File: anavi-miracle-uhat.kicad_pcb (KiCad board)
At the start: 2 copper layers, 65 x 30 mm, 25 parts, among them U1 CAT24C32WI-GT3, U2 74LVC1G17W5-7

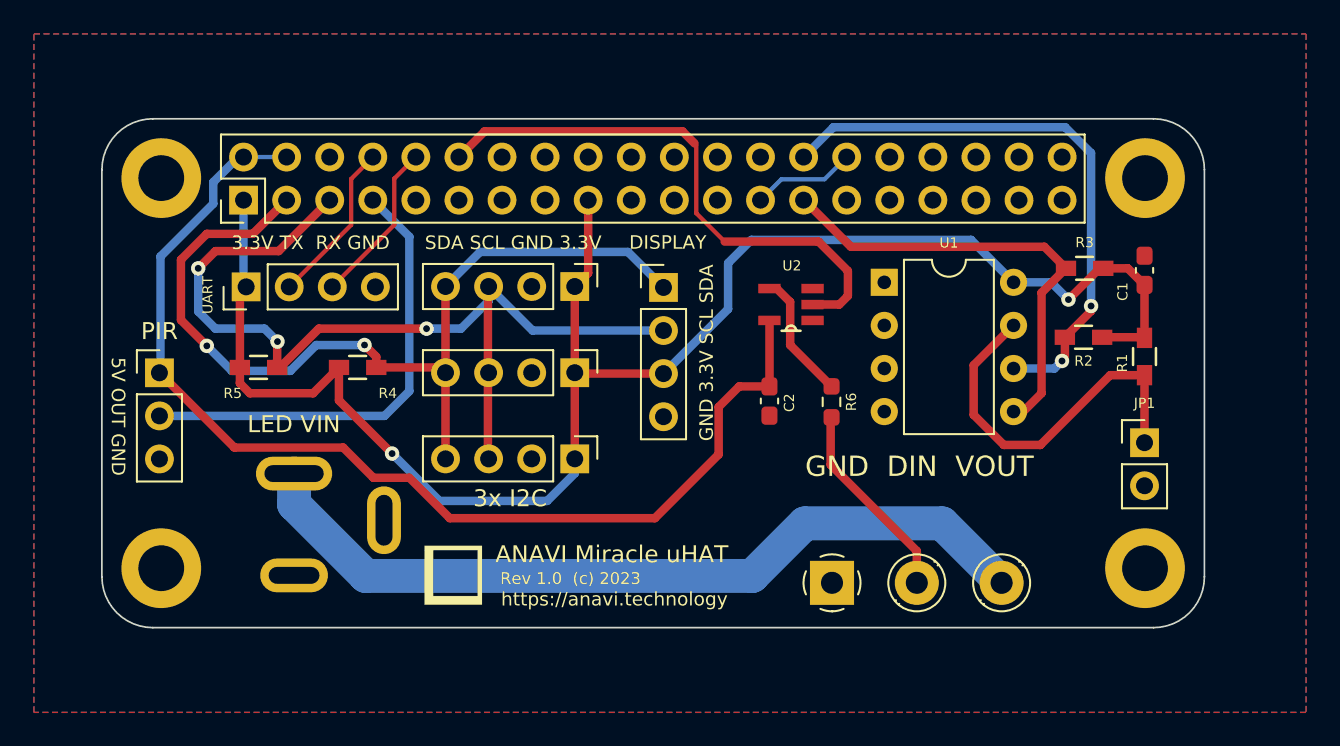
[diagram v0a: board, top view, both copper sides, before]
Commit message: anavi-miracle-uhat: Adjust LED strip connector
Adjust the addressable LED strip connector.

Signed-off-by: Leon Anavi <leon@anavi.org>
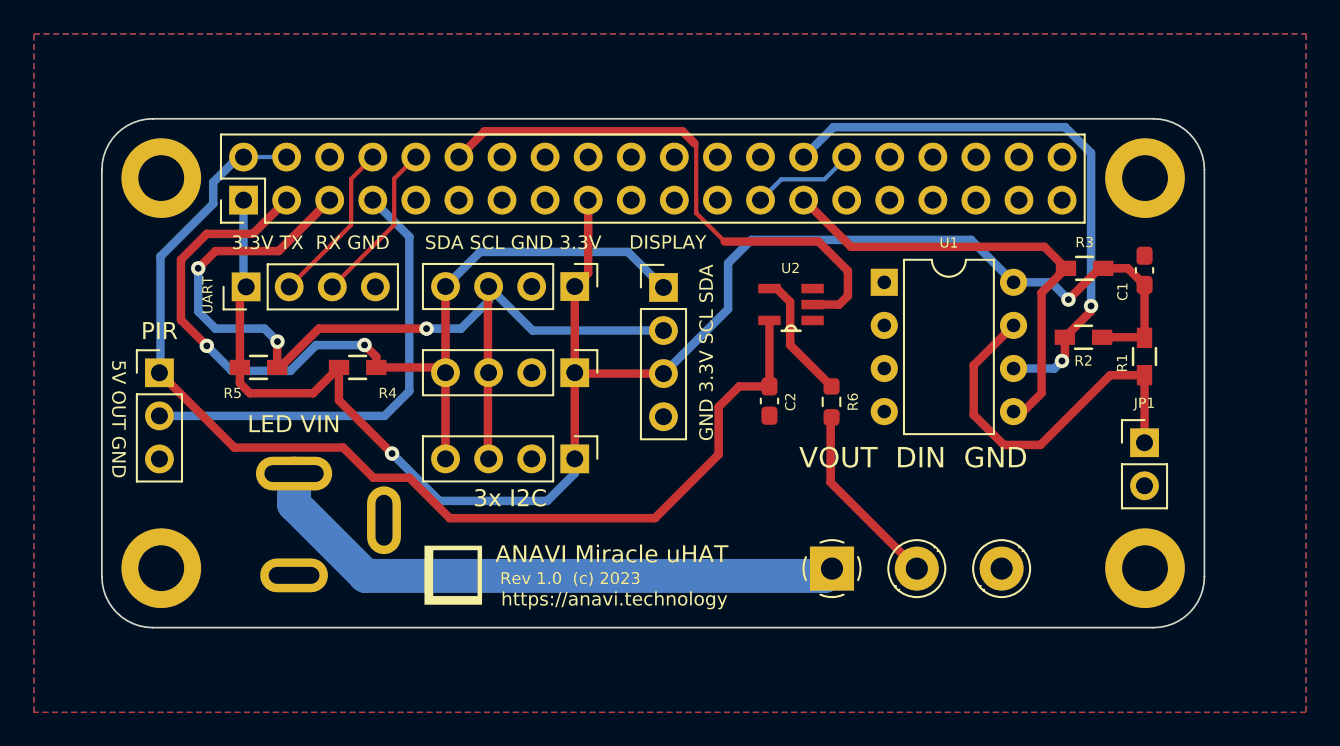
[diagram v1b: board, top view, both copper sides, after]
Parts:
- moved L1 0.84 mm to (191.5, 101.5)
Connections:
- L1 pad 1: GND -> Net-(DC1-Pad3)
- L1 pad 3: Net-(DC1-Pad3) -> GND
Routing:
- net Net-(DC1-Pad3): track 48.0 -> 35.5 mm
- net Net-(L1-Pad2): track 11.9 -> 11.0 mm
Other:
- board text added: "VOUT DIN GND"
- board text removed: "GND DIN VOUT"
